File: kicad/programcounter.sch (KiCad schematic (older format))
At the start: 6 parts, among them U13 74LS161, U14 74LS245

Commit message: Update to current kicad libraries
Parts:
- removed D18, D19, D20, D21: LED, LEDs:LED-5MM, symbol LED
- removed U13: 74LS161, Housings_DIP:DIP-16_W7.62mm_LongPads, symbol 74LS161
- removed U14: 74LS245, Housings_DIP:DIP-20_W7.62mm_LongPads, symbol 74LS245
- added D18, D19, D20, D21: LED, symbol Device:LED
- added U20: 74LS161, symbol 74xx:74LS161
- added U21: 74LS245, symbol 74xx:74LS245
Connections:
- net labels added: VCC
- wire segments 52 -> 58

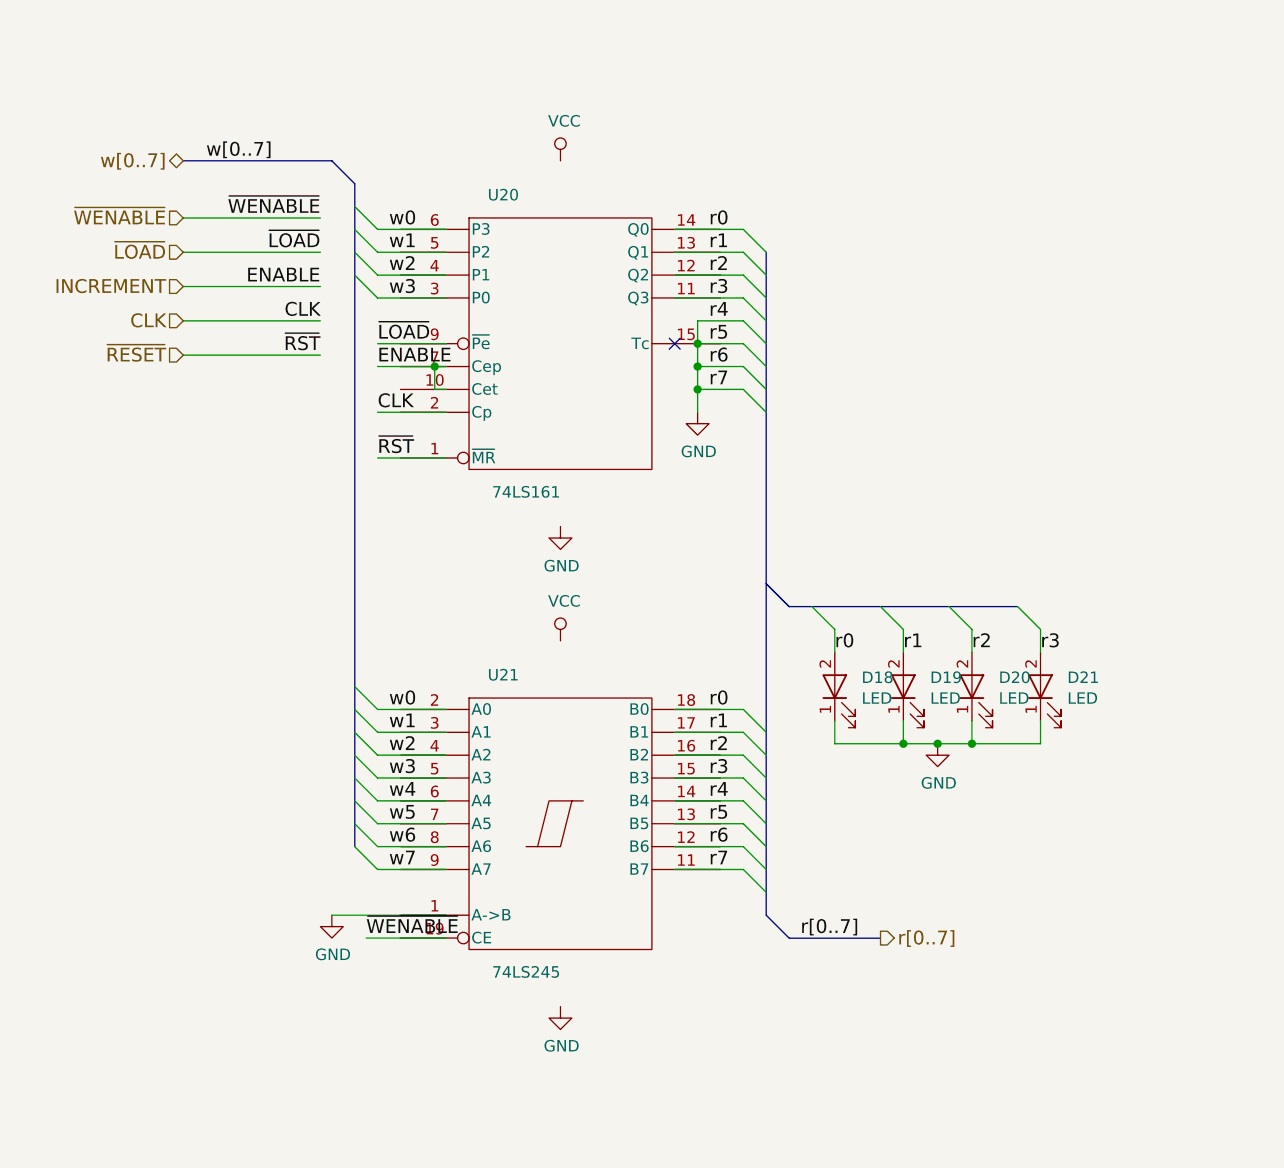
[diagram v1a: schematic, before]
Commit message: update bus names and improve sheet text
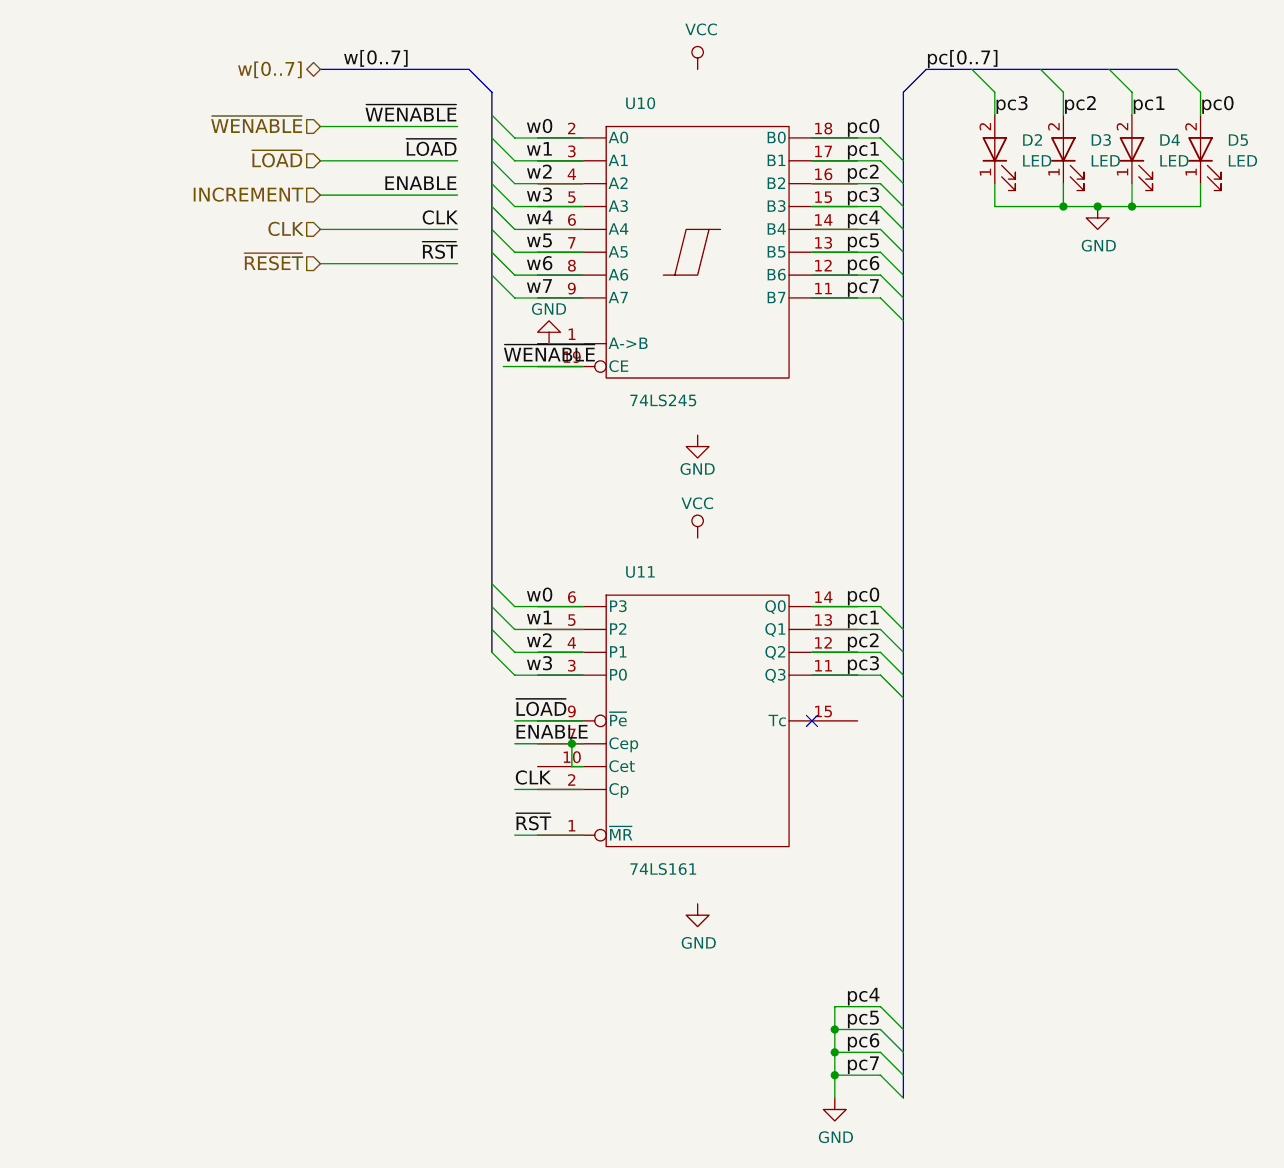
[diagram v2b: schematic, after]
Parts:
- renumbered D18 to D2, D19 to D3, D20 to D4, D21 to D5, U21 to U10, U20 to U11
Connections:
- net labels added: pc0, pc1, pc2, pc3, pc4, pc5, pc6, pc7, pc[0..7]
- net labels removed: r0, r1, r2, r3, r4, r5, r6, r7, r[0..7]
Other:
- moved on the sheet: D2, D3, D4, D5, U10, U11
